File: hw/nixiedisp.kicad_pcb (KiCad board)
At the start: 2 copper layers, 235 parts, among them J1 12VDC IN, J2 USB_B_Micro, J3 AVR-ISP-6, J4 pwr sw, Q1 MMBTA55, Q10 MMBTA42, Q11 MMBTA42, Q12 MMBTA42, Q13 MMBTA42, Q14 MMBTA42, Q15 MMBTA42, Q16 MMBTA42, Q17 MMBTA42, Q18 MMBTA42, Q19 MMBTA42, Q2 IRF540N, Q20 MMBTA42, Q21 MMBTA42, Q22 MMBTA42, Q23 MMBTA42, Q24 MMBTA42, Q25 MMBTA42, Q26 MMBTA42, Q27 MMBTA42, Q28 MMBTA42, Q29 MMBTA42, Q3 MMBTA42, Q30 MMBTA42, Q31 MMBTA42, Q32 MMBTA42, Q33 MMBTA42, Q34 MMBTA42, Q35 MMBTA42, Q36 MMBTA42, Q37 MMBTA42, Q38 MMBTA42, Q39 MMBTA42, Q4 MMBTA42, Q40 MMBTA42, Q41 MMBTA42, Q42 MMBTA42, Q43 MMBTA42, Q44 MMBTA42, Q45 MMBTA42, Q46 MMBTA42, Q47 MMBTA42, Q48 MMBTA42, Q49 MMBTA42, Q5 MMBTA42, Q50 MMBTA42, Q51 MMBTA42, Q52 MMBTA42, Q53 MMBTA42, Q54 MMBTA42, Q55 MMBTA42, Q56 MMBTA42, Q57 MMBTA42, Q58 MMBTA42, Q59 MMBTA42, Q6 MMBTA42, Q60 MMBTA42, Q61 MMBTA42, Q62 MMBTA42, Q63 MMBTA42, Q64 MMBTA42, Q65 MMBTA42, Q66 MMBTA42, Q67 MMBTA42, Q68 MMBTA42, Q7 MMBTA42, Q8 MMBTA42, Q9 MMBTA42, U1 ATmega328P-AU, U10 IN14, U11 IN14, U12 IN14, U13 IN14, U14 74HC154, U15 74HC04, U16 74HC04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

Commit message: PCB layout: nixie driver transistors and decoding pretty much final
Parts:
- C1, C15, C17, C20, C23, C26, C29, C32, Q10, Q11, Q12, Q13, Q14, Q15, Q16, Q17, Q18, Q19, Q20, Q21, Q22, Q23, Q24, Q25, Q26, Q27, Q28, Q29, Q3, Q30, Q31, Q32, Q33, Q34, Q35, Q36, Q37, Q38, Q39, Q4, Q40, Q41, Q42, Q43, Q44, Q45, Q46, Q47, Q48, Q49, Q5, Q50, Q51, Q52, Q53, Q54, Q55, Q56, Q57, Q58, Q59, Q6, Q60, Q61, Q62, Q63, Q64, Q65, Q66, Q67, Q68, Q7, Q8, Q9, R15, R16, R17, R18, R19, R20, R21, R22, R23, R24, R25, R26, R27, R28, R29, R30, R31, R32, R33, R34, R35, R36, R37, R38, R39, R40, R41, R42, R43, R44, R45, R46, R47, R48, R49, R50, R51, R52, R53, R54, R55, R56, R57, R58, R59, R60, R61, R62, R63, R64, R65, R66, R67, R68, R69, R70, R71, R72, R73, R74, R75, R76, R77, R78, R79, R80, R81, R82, R83, R84, R85, R86, R87, R88, R89, R90, R91, R92: moved to B.Cu
- moved R37 190.5 mm to (111.9, 160.0), turned to 180 degrees
- moved R31 184.8 mm to (116.1, 160.0), turned to 180 degrees
- moved Q16 182.2 mm to (108.5, 155.5), turned to 90 degrees
- moved R30 181.9 mm to (108.5, 159.3), turned to 270 degrees
- moved Q23 179.9 mm to (119.5, 155.5), turned to 90 degrees
- moved R38 169.7 mm to (119.5, 159.3), turned to 270 degrees
- moved Q22 169.2 mm to (112.0, 156.5), turned to 90 degrees
- moved Q17 166.5 mm to (116.0, 156.5), turned to 90 degrees
- moved Q20 165.3 mm to (111.5, 134.1), turned to 270 degrees
- moved R29 163.1 mm to (108.0, 126.7)
- moved C21 162.6 mm to (119.2, 132.1)
- moved R89 159.2 mm to (157.8, 160.0), turned to 180 degrees
- moved R35 158.1 mm to (111.5, 129.7), turned to 90 degrees
- moved Q18 156.3 mm to (122.0, 136.5), turned to 270 degrees
- moved R34 155.5 mm to (113.1, 126.2), turned to 180 degrees
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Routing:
- net VCC: track 0.00 -> 302.0 mm, vias 0 -> 12
- net Net-(R50-Pad2): track 0.00 -> 43.2 mm, vias 0 -> 1
- net Net-(R37-Pad2): track 0.00 -> 43.2 mm, vias 0 -> 1
- net Net-(R24-Pad2): track 0.00 -> 43.2 mm, vias 0 -> 1
- net Net-(R89-Pad2): track 0.00 -> 43.2 mm, vias 0 -> 1
- net Net-(R76-Pad2): track 0.00 -> 43.2 mm, vias 0 -> 1
- net Net-(R63-Pad2): track 0.00 -> 43.2 mm, vias 0 -> 1
- net Net-(R30-Pad2): track 0.00 -> 41.5 mm, vias 0 -> 1
- net Net-(R17-Pad2): track 0.00 -> 41.5 mm, vias 0 -> 1
- net Net-(R82-Pad2): track 0.00 -> 41.5 mm, vias 0 -> 1
- net Net-(R69-Pad2): track 0.00 -> 41.5 mm, vias 0 -> 1
- net Net-(R56-Pad2): track 0.00 -> 41.5 mm, vias 0 -> 1
- net Net-(R43-Pad2): track 0.00 -> 41.5 mm, vias 0 -> 1
- net Net-(R31-Pad2): track 0.00 -> 41.0 mm, vias 0 -> 1
- net Net-(R18-Pad2): track 0.00 -> 41.0 mm, vias 0 -> 1
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
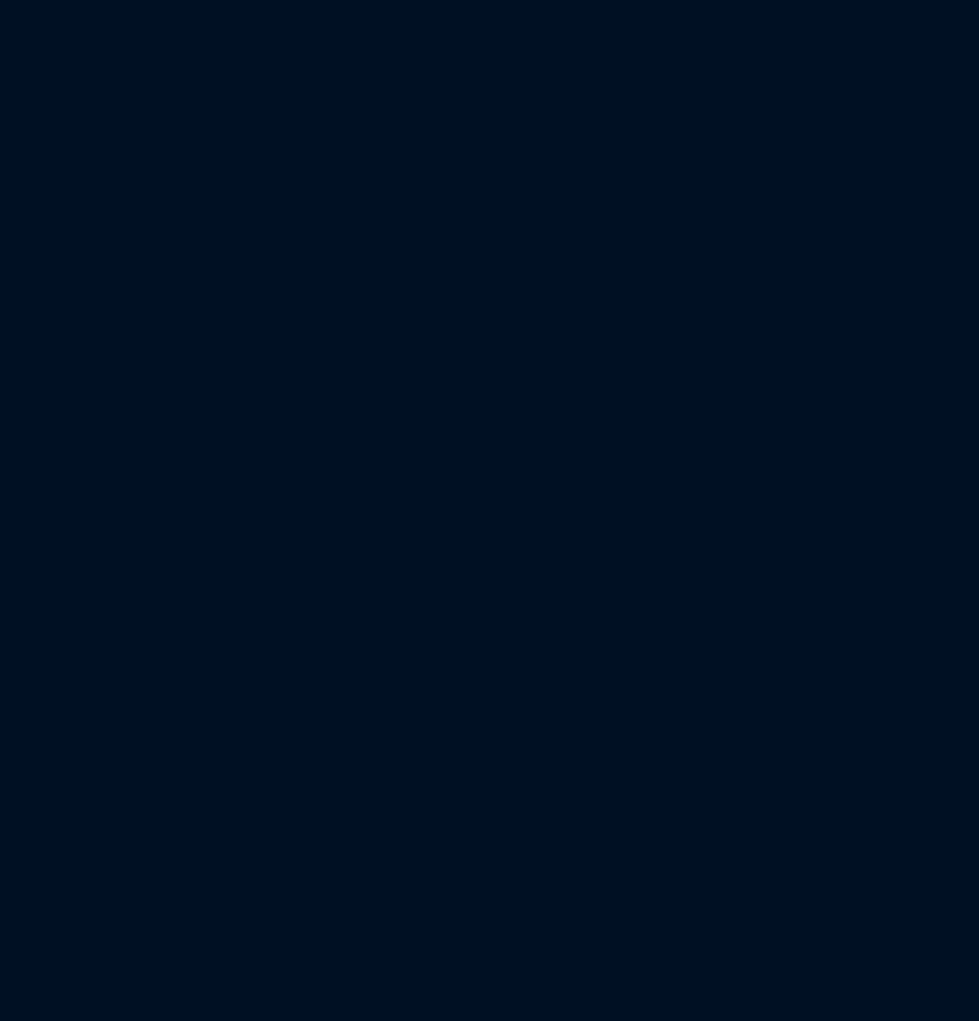
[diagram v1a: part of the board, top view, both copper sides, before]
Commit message: added RTC to the schematic
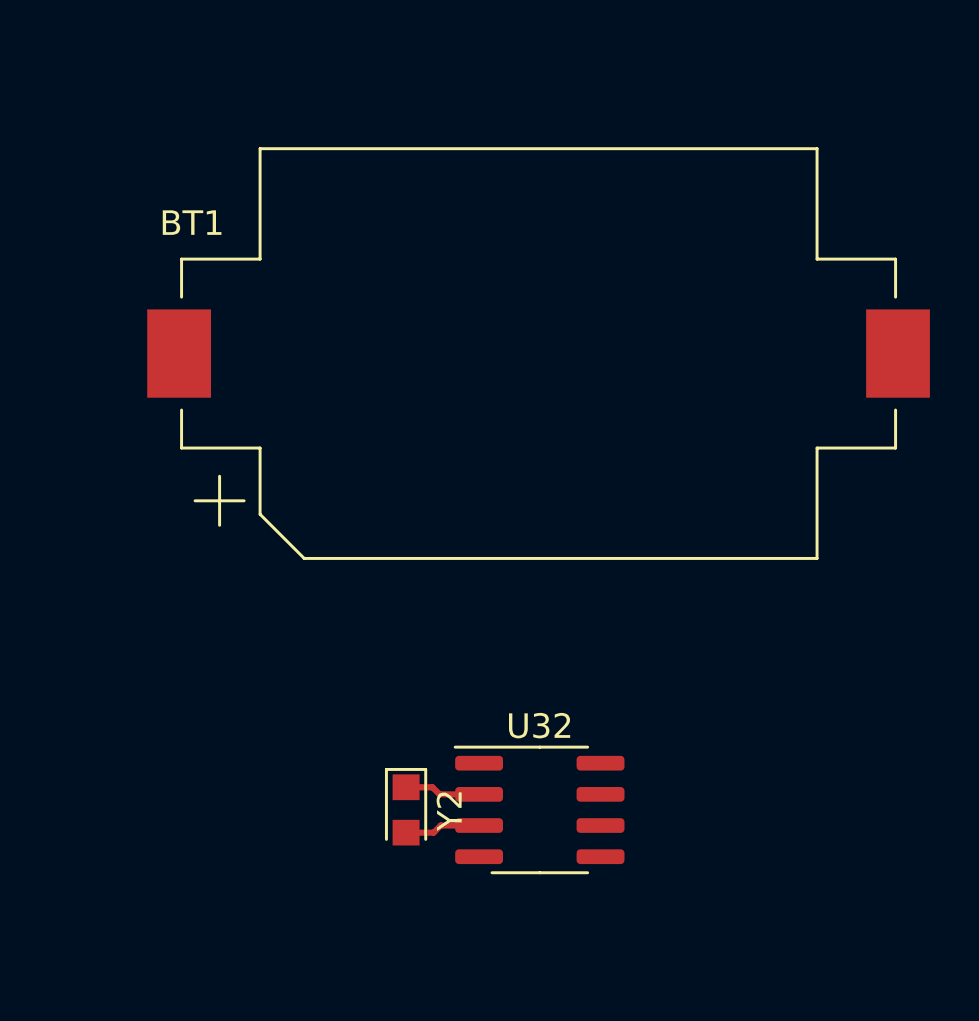
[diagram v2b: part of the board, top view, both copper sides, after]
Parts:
- added BT1: 3V, Battery:BatteryHolder_Keystone_1060_1x2032, F.Cu at (222.4, -9.60)
- added U32: DS1302Z+, Package_SO:SOIC-8_3.9x4.9mm_P1.27mm, F.Cu at (222.5, 9.00)
- added Y2: 32.768KHz, Crystal:Crystal_SMD_2012-2Pin_2.0x1.2mm_HandSoldering, F.Cu at (217.1, 9.00)
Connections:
- U1 pad 25: (no net) -> /RTC_CE
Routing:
- net Net-(U32-Pad3): track 0.00 -> 3.10 mm
- net Net-(U32-Pad2): track 0.00 -> 3.10 mm

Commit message: PCB layout almost done
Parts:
- removed D2: LEDBOT, LED_SMD:LED_0805_2012Metric_Pad1.15x1.40mm_HandSolder
- removed D3: LEDTOP, LED_SMD:LED_0805_2012Metric_Pad1.15x1.40mm_HandSolder
- added J5: HRLEDS, Connector_PinSocket_2.54mm:PinSocket_1x03_P2.54mm_Vertical, F.Cu at (125.5, 141.8)
- added REF**: M3, MountingHole:MountingHole_3.2mm_M3_Pad_Via, F.Cu at (214.0, 161.1)
- added REF**: M3, MountingHole:MountingHole_3.2mm_M3_Pad_Via, F.Cu at (214.0, 76.0)
- added REF**: M3, MountingHole:MountingHole_3.2mm_M3_Pad_Via, F.Cu at (167.0, 76.0)
- added REF**: M3, MountingHole:MountingHole_3.2mm_M3_Pad_Via, F.Cu at (167.0, 161.1)
- added REF**: M3, MountingHole:MountingHole_3.2mm_M3_Pad_Via, F.Cu at (83.0, 76.0)
- added REF**: M3, MountingHole:MountingHole_3.2mm_M3_Pad_Via, F.Cu at (83.0, 161.1)
- added Y3: 32.768KHz, Crystal:Crystal_C38-LF_D3.0mm_L8.0mm_Horizontal, F.Cu at (122.0, 77.2)
- BT1, C10, C9, R7, R8: moved to B.Cu
- moved C8 177.5 mm to (106.3, 96.8), turned to 270 degrees
- moved C16 165.2 mm to (82.5, 101.7), turned to 0 degrees
- moved D4 164.7 mm to (82.5, 96.2), turned to 90 degrees
- moved R1 158.6 mm to (104.2, 88.2)
- moved L1 156.2 mm to (97.2, 88.5), turned to 90 degrees
- moved C1 152.6 mm to (94.0, 99.7)
- moved C15 152.6 mm to (96.7, 102.2)
- moved U2 152.6 mm to (91.5, 93.5)
- moved U3 150.6 mm to (118.1, 83.5), turned to 270 degrees
- moved J4 148.9 mm to (117.0, 76.8), turned to 180 degrees
- moved D1 148.5 mm to (88.8, 95.0), turned to 270 degrees
- moved U7 145.7 mm to (194.5, 100.6)
- moved Q1 145.6 mm to (88.8, 89.2), turned to 90 degrees
- moved C2 145.5 mm to (112.8, 89.0), turned to 270 degrees
- moved Q2 144.5 mm to (92.8, 77.7)
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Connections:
- net Net-(BT1-Pad1) renamed /VBATT
- R5 pad 1: GND -> Net-(J5-Pad2)
- R5 pad 2: Net-(D2-Pad1) -> /HRSEP
- R6 pad 1: GND -> Net-(J5-Pad1)
- R6 pad 2: Net-(D3-Pad1) -> /HRSEP
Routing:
- net VCC: track 302.0 -> 583.5 mm, vias 12 -> 14
- net HT: track 0.00 -> 210.1 mm, vias 0 -> 6
- net /FDOT: track 1.63 -> 113.7 mm, vias 1 -> 3
- net /SD: track 0.00 -> 90.6 mm
- net /CK3: track 0.00 -> 89.9 mm, vias 0 -> 2
- net /EDOT: track 1.63 -> 89.2 mm, vias 1 -> 3
- net /DDOT: track 1.63 -> 63.3 mm, vias 1 -> 3
- net /ADOT: track 1.63 -> 61.5 mm, vias 1 -> 3
- net Net-(J5-Pad2): track 0.00 -> 47.1 mm, vias 0 -> 1
- net /~RST: track 0.00 -> 45.9 mm, vias 0 -> 1
- net Net-(J5-Pad1): track 0.00 -> 44.1 mm, vias 0 -> 1
- net +12V: track 0.00 -> 43.8 mm
- net /BDOT: track 1.63 -> 39.0 mm, vias 1 -> 3
- net /CDOT: track 1.63 -> 39.0 mm, vias 1 -> 3
- net /A0: track 0.00 -> 34.7 mm
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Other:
- board outline added: 140 x 94.1 mm

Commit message: finished the PCB rev1
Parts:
- added G***: LOGO, nixiedisp:gnulogo, F.Cu at (194.6, 82.8)
- added G***: LOGO, nixiedisp:gnulogo, F.Cu at (158.7, 100.0)
- added REF**: Symbol_Barrel_Polarity, Symbol:Symbol_Barrel_Polarity, F.Cu at (107.8, 85.0)
- J1: value 12VDC IN -> 12V DC
- J3: value AVR-ISP-6 -> AVRISP
- U1: value ATmega328P-AU -> ATmega328P
- U3: value L7805 -> 7805
- U4: value MCP2221AxSL -> MCP2221A
- moved REF** 0.50 mm to (167.5, 76.0)
- moved REF** 0.50 mm to (167.5, 161.1)
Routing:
- net GND: track 0.14 -> 57.0 mm, vias 0 -> 146
- net VCC: track 583.5 -> 599.7 mm, vias 14 -> 15
- net /ADOT: track 61.5 -> 62.7 mm
- net Net-(U29-Pad8): track 14.0 -> 12.9 mm
- net /DDOT: track 63.3 -> 62.3 mm
- net Net-(U20-Pad8): track 14.0 -> 13.0 mm
- net Net-(U23-Pad8): track 14.0 -> 13.0 mm
- net Net-(U26-Pad8): track 14.0 -> 13.1 mm
- net /TXD: track 26.7 -> 25.9 mm
- net /RXD: track 29.0 -> 28.2 mm
- net Net-(J2-Pad3): track 12.7 -> 11.9 mm
- net /CK2: track 34.0 -> 34.8 mm
- net Net-(Q51-Pad1): track 10.4 -> 11.2 mm
- net Net-(Q7-Pad1): track 10.4 -> 11.2 mm
- net Net-(U14-Pad8): track 14.0 -> 13.3 mm
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- added copper zone on B.Cu, net GND
- added copper zone on F.Cu, net GND
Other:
- board text added: "<nuclear@member.fsf.org>"
- board text added: "Bottom half: - All unmarked resistors: 47 kOhm - All transistors: MMBTA42"
- board text added: "CAUTION 120 V"
- board text added: "CAUTION High Voltage"
- board text added: "CR2032"
- board text added: "Copyright © 2020 John Tsiombikas"
- board text added: "Cut along the line for a 4-digit display"
- board text added: "Free hw design GNU GPLv3 or later"
- board text added: "USB nixie display"
- board text added: "Use soviet ИH-14 nixie tubes"
- board text added: "https://github.com/jtsiomb/nixiedisp"
- board text added: "ИH-14"

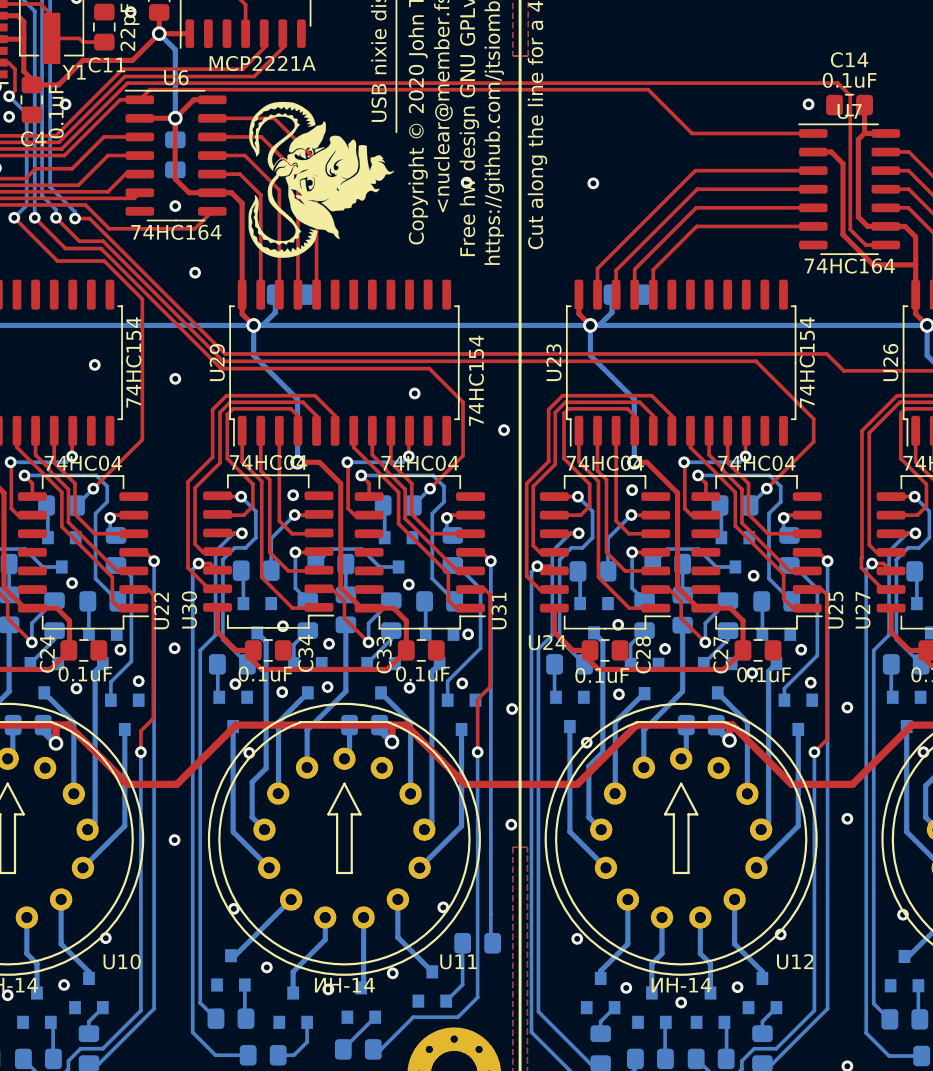
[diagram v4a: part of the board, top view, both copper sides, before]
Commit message: minor pcb adjustments
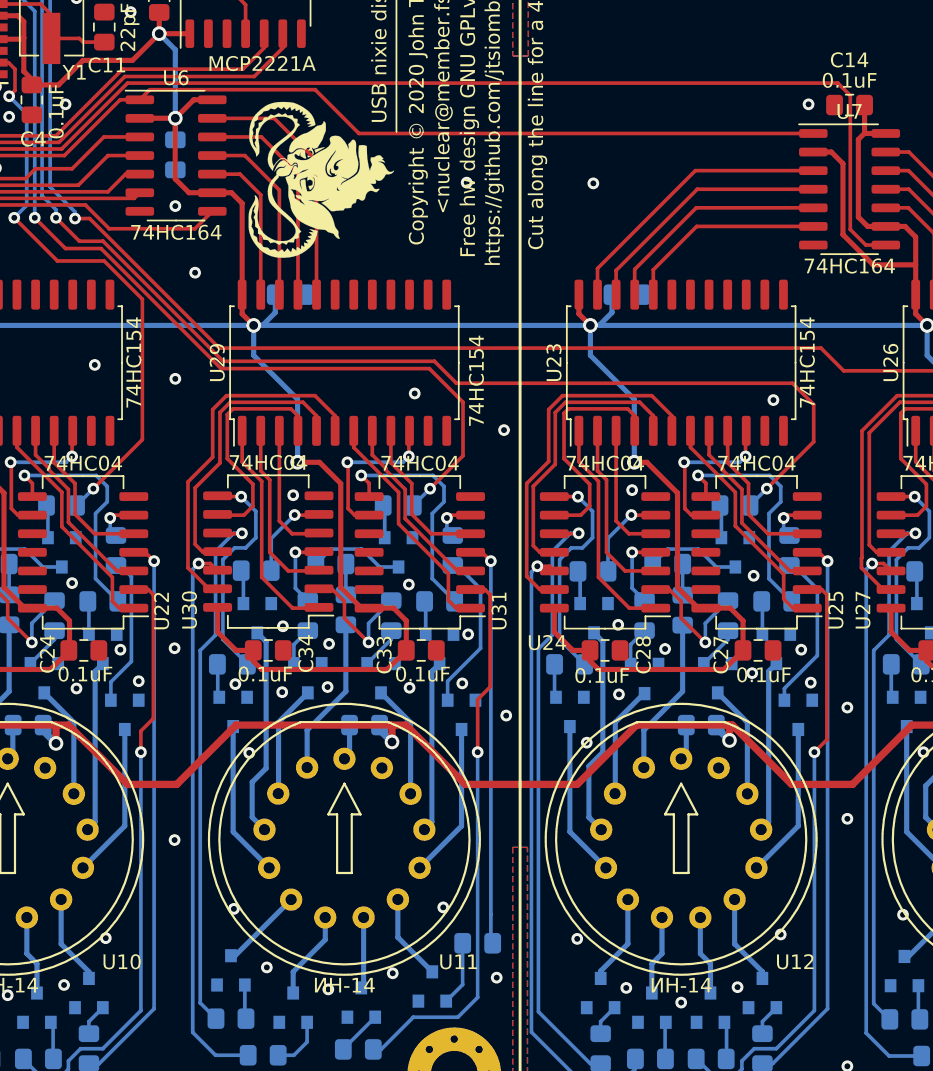
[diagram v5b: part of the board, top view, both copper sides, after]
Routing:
- net /EDOT: track 89.2 -> 89.8 mm
- net GND: vias 146 -> 147

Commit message: - fixed mistakes in the schematic - updated the PCB for the fixes - in process of adding a proper serial port with a max232
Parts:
- removed the G*** at (194.6, 82.8)
- removed the G*** at (158.7, 100.0)
- removed the REF** at (214.0, 161.1)
- removed the REF** at (214.0, 76.0)
- removed the REF** at (167.5, 76.0)
- removed the REF** at (167.5, 161.1)
- removed the REF** at (83.0, 76.0)
- removed the REF** at (83.0, 161.1)
- added C35: 0.33uF, Capacitor_SMD:CP_Elec_4x5.4, F.Cu at (115.0, 63.0)
- added G***: LOGO, nixiedisp:gnulogo, F.Cu at (148.7, 80.0)
- added REF**: M3, MountingHole:MountingHole_3.2mm_M3_Pad_Via, F.Cu at (204.0, 141.1)
- added REF**: M3, MountingHole:MountingHole_3.2mm_M3_Pad_Via, F.Cu at (204.0, 56.0)
- added REF**: M3, MountingHole:MountingHole_3.2mm_M3_Pad_Via, F.Cu at (157.5, 56.0)
- added REF**: M3, MountingHole:MountingHole_3.2mm_M3_Pad_Via, F.Cu at (157.5, 141.1)
- added REF**: M3, MountingHole:MountingHole_3.2mm_M3_Pad_Via, F.Cu at (73.0, 56.0)
- added REF**: M3, MountingHole:MountingHole_3.2mm_M3_Pad_Via, F.Cu at (73.0, 141.1)
- C16: value 2.2uF -> 2.2uF 250V
- J1: value 12V DC -> 12VDC IN
- J3: value AVRISP -> AVR-ISP-6
- Q2: value IRF540N -> IRF740
- U1: value ATmega328P -> ATmega328P-AU
- U3: value 7805 -> L7805
- U4: value MCP2221A -> MCP2221AxSL
- moved J5 34.0 mm to (115.5, 109.3)
- moved Q18 22.5 mm to (111.7, 116.5)
- moved U19 22.5 mm to (108.9, 105.4)
- moved Q10 22.4 mm to (73.4, 116.3)
- moved Q14 22.4 mm to (106.5, 114.0)
- moved Q20 22.4 mm to (101.5, 114.0)
- moved Q21 22.4 mm to (96.4, 116.3)
- moved Q42 22.4 mm to (170.5, 114.0)
- moved Q43 22.4 mm to (165.4, 116.3)
- moved Q54 22.4 mm to (188.4, 116.3)
- moved Q65 22.4 mm to (142.4, 116.3)
- moved R23 22.4 mm to (73.4, 113.0)
- moved R36 22.4 mm to (96.4, 113.0)
- moved R49 22.4 mm to (119.4, 113.0)
- moved R62 22.4 mm to (165.4, 113.0)
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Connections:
- J2 pad 1: (no net) -> Net-(J2-Pad1)
- J2 pad 4: (no net) -> Net-(J2-Pad4)
- Q1 pad 2: GND -> Net-(D1-Pad1)
- Q1 pad 3: Net-(D1-Pad1) -> GND
- U1 pad 19: (no net) -> Net-(U1-Pad19)
- U1 pad 20: (no net) -> Net-(U1-Pad20)
- U1 pad 22: (no net) -> Net-(U1-Pad22)
- U1 pad 26: (no net) -> Net-(U1-Pad26)
- U1 pad 27: (no net) -> Net-(U1-Pad27)
- U1 pad 28: (no net) -> Net-(U1-Pad28)
- U10 pad 13: (no net) -> Net-(U10-Pad13)
- U11 pad 13: (no net) -> Net-(U11-Pad13)
- U12 pad 13: (no net) -> Net-(U12-Pad13)
- U13 pad 13: (no net) -> Net-(U13-Pad13)
- U14 pad 11: (no net) -> Net-(U14-Pad11)
- U14 pad 13: (no net) -> Net-(U14-Pad13)
- U14 pad 14: (no net) -> Net-(U14-Pad14)
- U14 pad 15: (no net) -> Net-(U14-Pad15)
- U14 pad 16: (no net) -> Net-(U14-Pad16)
- U14 pad 17: (no net) -> Net-(U14-Pad17)
- U16 pad 10: (no net) -> Net-(U16-Pad10)
- U16 pad 12: (no net) -> Net-(U16-Pad12)
- U17 pad 11: (no net) -> Net-(U17-Pad11)
- U17 pad 13: (no net) -> Net-(U17-Pad13)
- U17 pad 14: (no net) -> Net-(U17-Pad14)
- U17 pad 15: (no net) -> Net-(U17-Pad15)
- U17 pad 16: (no net) -> Net-(U17-Pad16)
- U17 pad 17: (no net) -> Net-(U17-Pad17)
- U19 pad 10: (no net) -> Net-(U19-Pad10)
- U19 pad 12: (no net) -> Net-(U19-Pad12)
- U20 pad 11: (no net) -> Net-(U20-Pad11)
- U20 pad 13: (no net) -> Net-(U20-Pad13)
- U20 pad 14: (no net) -> Net-(U20-Pad14)
- U20 pad 15: (no net) -> Net-(U20-Pad15)
- U20 pad 16: (no net) -> Net-(U20-Pad16)
- U20 pad 17: (no net) -> Net-(U20-Pad17)
- U22 pad 10: (no net) -> Net-(U22-Pad10)
- U22 pad 12: (no net) -> Net-(U22-Pad12)
- U23 pad 11: (no net) -> Net-(U23-Pad11)
- U23 pad 13: (no net) -> Net-(U23-Pad13)
- U23 pad 14: (no net) -> Net-(U23-Pad14)
- U23 pad 15: (no net) -> Net-(U23-Pad15)
- U23 pad 16: (no net) -> Net-(U23-Pad16)
- U23 pad 17: (no net) -> Net-(U23-Pad17)
- U25 pad 10: (no net) -> Net-(U25-Pad10)
- U25 pad 12: (no net) -> Net-(U25-Pad12)
- U26 pad 11: (no net) -> Net-(U26-Pad11)
- U26 pad 13: (no net) -> Net-(U26-Pad13)
- U26 pad 14: (no net) -> Net-(U26-Pad14)
- U26 pad 15: (no net) -> Net-(U26-Pad15)
- U26 pad 16: (no net) -> Net-(U26-Pad16)
- U26 pad 17: (no net) -> Net-(U26-Pad17)
- U28 pad 10: (no net) -> Net-(U28-Pad10)
- U28 pad 12: (no net) -> Net-(U28-Pad12)
- U29 pad 11: (no net) -> Net-(U29-Pad11)
- U29 pad 13: (no net) -> Net-(U29-Pad13)
- U29 pad 14: (no net) -> Net-(U29-Pad14)
- U29 pad 15: (no net) -> Net-(U29-Pad15)
- U29 pad 16: (no net) -> Net-(U29-Pad16)
- U29 pad 17: (no net) -> Net-(U29-Pad17)
- U31 pad 10: (no net) -> Net-(U31-Pad10)
- U31 pad 12: (no net) -> Net-(U31-Pad12)
- U4 pad 10: (no net) -> Net-(U4-Pad10)
- U4 pad 2: (no net) -> Net-(U4-Pad2)
- U4 pad 3: (no net) -> Net-(U4-Pad3)
- U4 pad 7: (no net) -> Net-(U4-Pad7)
- U4 pad 8: (no net) -> Net-(U4-Pad8)
- U4 pad 9: (no net) -> Net-(U4-Pad9)
- U8 pad 13: (no net) -> Net-(U8-Pad13)
- U9 pad 13: (no net) -> Net-(U9-Pad13)
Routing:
- net Net-(J5-Pad1): track 44.1 -> 31.7 mm
- net Net-(J5-Pad2): track 47.1 -> 34.7 mm
- net GND: track 57.0 -> 62.6 mm, vias 147 -> 148
- net HT: track 210.1 -> 213.4 mm
- net Net-(D1-Pad2): track 14.3 -> 16.1 mm
- net Net-(U20-Pad10): track 10.9 -> 11.9 mm
- net VCC: track 599.7 -> 598.8 mm
- net Net-(D1-Pad1): track 18.0 -> 18.8 mm
- net Net-(U17-Pad10): track 10.9 -> 11.7 mm
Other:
- board text added: "CAUTION 180 V"
- board text removed: "CAUTION 120 V"
